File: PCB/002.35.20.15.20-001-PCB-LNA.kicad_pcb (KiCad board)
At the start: 4 copper layers, 52.5 x 40.5 mm, 36 parts, among them U1 PMA2-63LN+, U2 PMA2-63LN+, U3 YAT-1A+, U4 L7805, U5 L7805

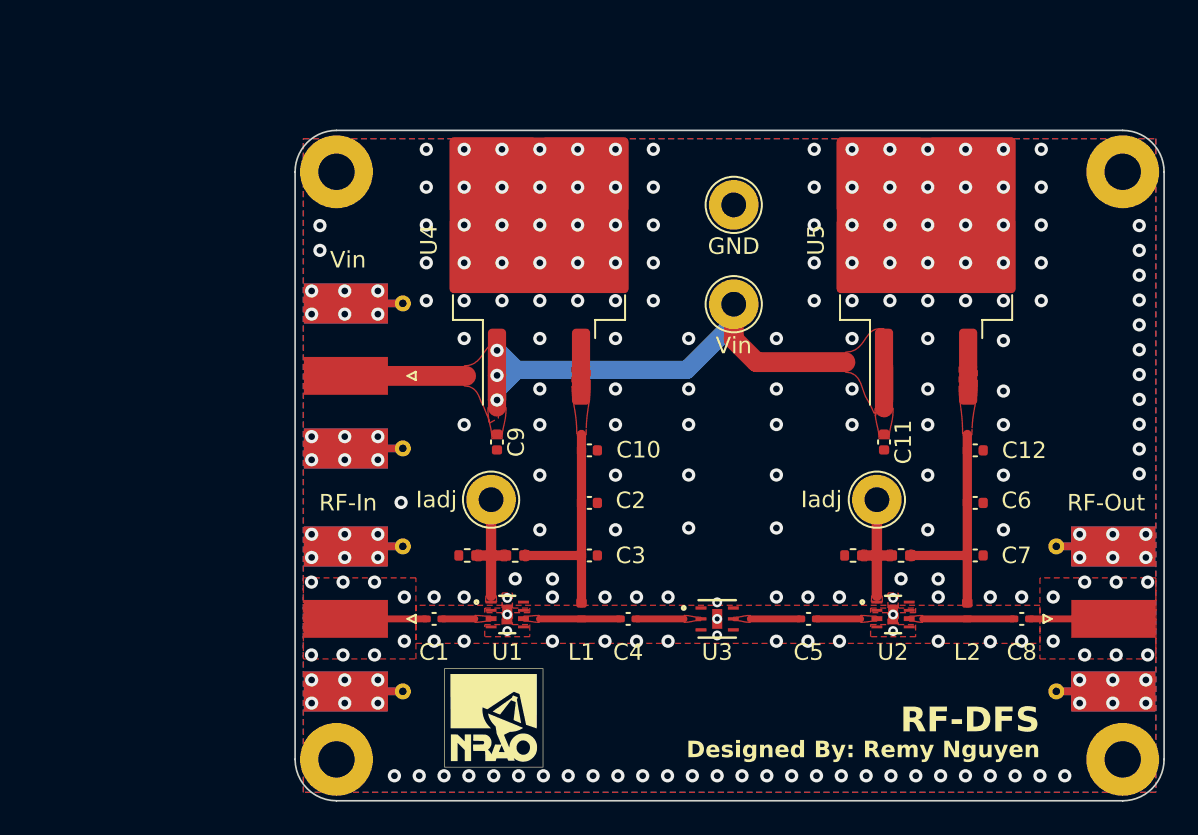
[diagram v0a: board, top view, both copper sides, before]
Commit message: Assembly drawing updated
* New stackup table format
* SMA dimensions adjusted to appease mechanicals (it's not technically accurate)
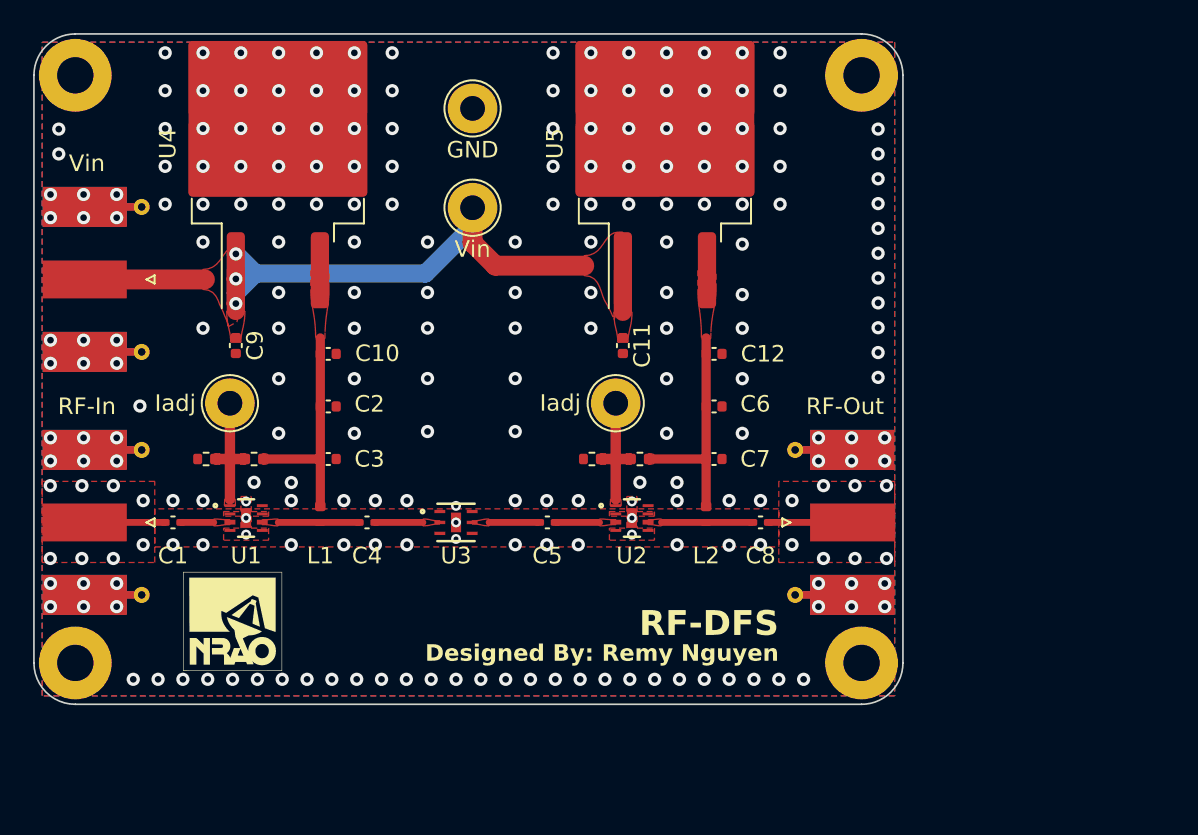
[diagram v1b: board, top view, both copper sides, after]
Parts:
- added REF**: FabDrawing-4Layer, FabDrawingTemplates:FabDrawing-4Layer-Metric-Compact, F.Cu at (55.0, 133.0)
- moved C5 16.8 mm to (113.2, 88.7)
- moved L2 16.8 mm to (122.8, 88.2)
- moved RF-Out 16.8 mm to (129.9, 88.7)
- moved R4 16.8 mm to (118.8, 84.9)
- moved U5 16.8 mm to (120.3, 65.8)
- moved C1 16.8 mm to (90.6, 88.7)
- moved C4 16.8 mm to (102.3, 88.7)
- moved C8 16.8 mm to (126.1, 88.7)
- moved C9 16.8 mm to (94.4, 78.0)
- moved L1 16.8 mm to (99.5, 88.2)
- moved RF-In 16.8 mm to (87.0, 88.7)
- moved U1 16.8 mm to (95.0, 88.4)
- moved U2 16.8 mm to (118.3, 88.4)
- moved U3 16.8 mm to (107.7, 88.7)
- moved GND 16.8 mm to (108.7, 63.7)
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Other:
- board text removed: "0"
- board text removed: "0 mm"
- board text removed: "0.0098"
- board text removed: "0.01"
- board text removed: "0.0175 mm"
- board text removed: "0.0254 mm"
- board text removed: "0.0432 mm"
- board text removed: "0.2021 mm"
- board text removed: "0.9906 mm"
- board text removed: "1"
- board text removed: "3.3"
- board text removed: "3.6"
- board text removed: "3.64"
- board text removed: "B.Cu"
- board text removed: "B.Mask"
- board text removed: "B.Paste"
- board text removed: "B.Silkscreen"
- board text removed: "Bottom Silk Screen"
- board text removed: "Bottom Solder Mask"
- board text removed: "Bottom Solder Paste"
- board text removed: "Color"
- board text removed: "Dielectric 1"
- board text removed: "Dielectric 2"
- board text removed: "Dielectric 3"
- board text removed: "Epsilon R"
- board text removed: "F.Cu"
- board text removed: "F.Mask"
- board text removed: "F.Paste"
- board text removed: "F.Silkscreen"
- board text removed: "FR4 natural"
- board text removed: "FR408-HR"
- board text removed: "FR408HR 2113"
- board text removed: "In1.Cu"
- board text removed: "In2.Cu"
- board text removed: "Layer Name"
- board text removed: "Liquid Ink"
- board text removed: "Liquid Photo"
- board text removed: "Loss Tangent"
- board text removed: "Material"
- board text removed: "Purple"
- board text removed: "Thickness (mm)"
- board text removed: "Top Silk Screen"
- board text removed: "Top Solder Mask"
- board text removed: "Top Solder Paste"
- board text removed: "Type"
- board text removed: "White"
- board text removed: "copper"
- board text removed: "core"
- board text removed: "prepreg"
